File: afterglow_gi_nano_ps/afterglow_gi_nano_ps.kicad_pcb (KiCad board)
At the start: 2 copper layers, 84 x 134.5 mm, 70 parts, among them J1 Conn_02x17_Odd_Even, J2 POWER_CONN, J3 GI_WPC_J120, J4 GI_WPC_J121, J5 GI_CONN_J119, J6 Conn_01x12_Male, Q1 FQP30N06L, Q2 FQP30N06L, Q3 FQP30N06L, Q4 FQP30N06L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

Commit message: Added 5V stabilizing capacitor
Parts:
- added C9: 100uF, Capacitors_THT:CP_Radial_D8.0mm_P3.50mm, F.Cu at (119.5, 41.0)
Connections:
- REF** pad 1: (no net) -> GND (x2)

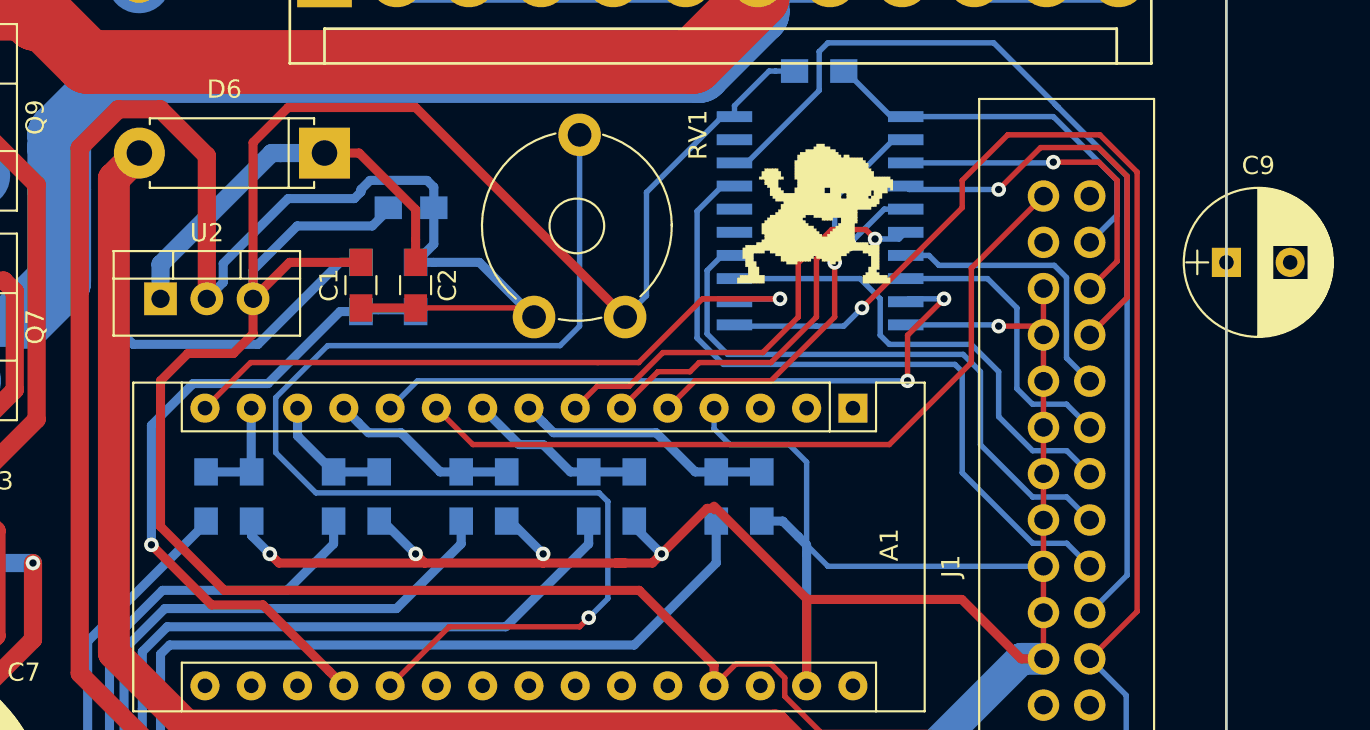
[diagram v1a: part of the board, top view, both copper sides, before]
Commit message: Added 5V stabilizing capacitor
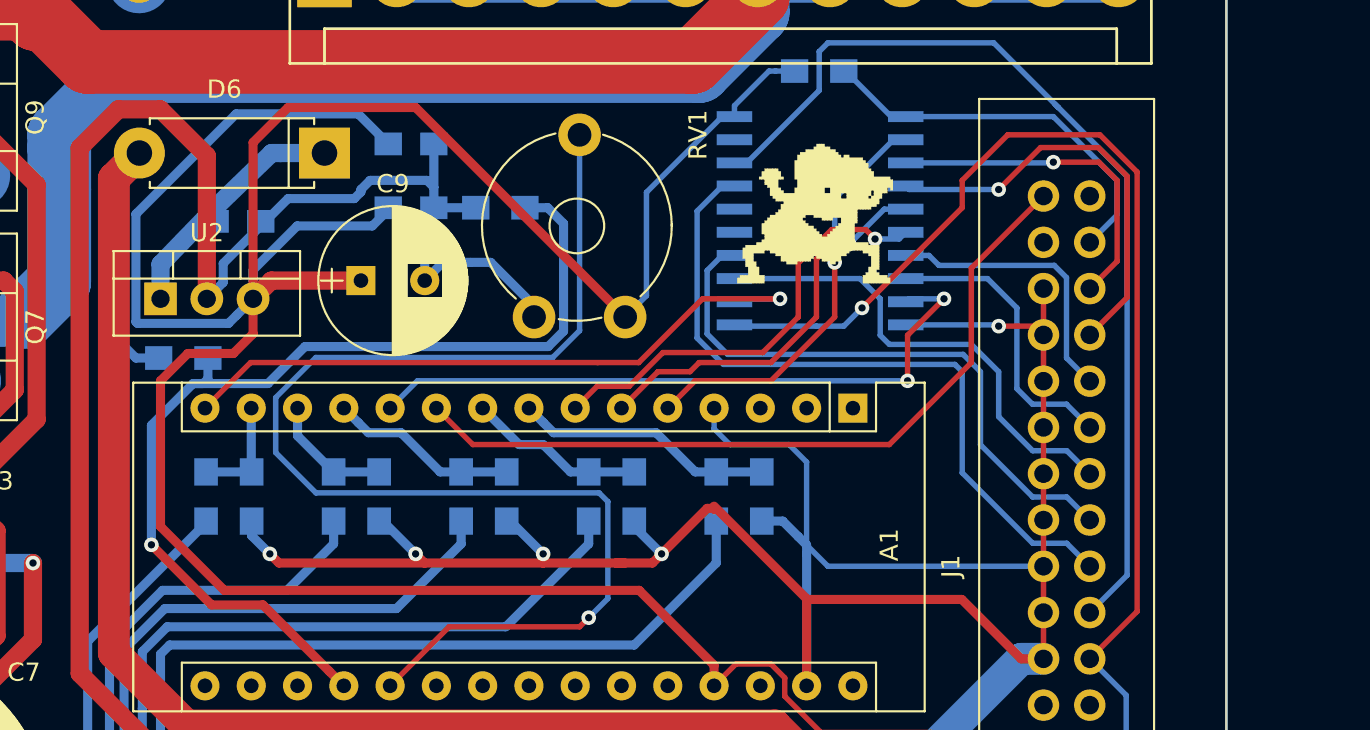
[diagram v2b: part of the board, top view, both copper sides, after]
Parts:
- C1, C2: moved to B.Cu
- moved C9 47.5 mm to (72.0, 42.0)
- moved R23 10.5 mm to (62.2, 46.2), turned to 0 degrees
- moved C2 10.4 mm to (65.2, 38.8), turned to 0 degrees
- moved C1 8.22 mm to (74.8, 34.5), turned to 180 degrees
- moved R24 6.37 mm to (79.7, 38.0), turned to 180 degrees
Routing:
- net /5V: track 152.7 -> 182.1 mm
- net Net-(A1-Pad19): track 37.4 -> 55.5 mm
- net +12V: track 574.0 -> 561.7 mm
- net Net-(C2-Pad1): track 22.6 -> 14.9 mm
- net GND: track 539.5 -> 535.8 mm

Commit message: Added PS BOM and schematic
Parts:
- C4: value C -> 1uF
- C5, C6, C7, C8: value CP -> 5600uF
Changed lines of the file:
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@@
       (effects (font (size 1 1) (thickness 0.15)))
     )
-    (fp_text value C (at 2.5 3.06 90) (layer F.Fab)
+    (fp_text value 1uF (at 2.5 3.06 90) (layer F.Fab)
       (effects (font (size 1 1) (thickness 0.15)))
     )
@@
       (effects (font (size 1 1) (thickness 0.15)))
     )
-    (fp_text value CP (at 3.75 10.31) (layer F.Fab)
+    (fp_text value 5600uF (at 3.75 10.31) (layer F.Fab)
       (effects (font (size 1 1) (thickness 0.15)))
     )
@@
       (effects (font (size 1 1) (thickness 0.15)))
     )
-    (fp_text value CP (at 3.75 10.31) (layer F.Fab)
+    (fp_text value 5600uF (at 3.75 10.31) (layer F.Fab)
       (effects (font (size 1 1) (thickness 0.15)))
     )
@@
       (effects (font (size 1 1) (thickness 0.15)))
     )
-    (fp_text value CP (at 3.75 10.31) (layer F.Fab)
+    (fp_text value 5600uF (at 3.75 10.31) (layer F.Fab)
       (effects (font (size 1 1) (thickness 0.15)))
     )
@@
       (effects (font (size 1 1) (thickness 0.15)))
     )
-    (fp_text value CP (at 3.75 10.31) (layer F.Fab)
-      (effects (font (size 1 1) (thickness 0.15)))
-    )
+    (fp_text value 5600uF (at 3.75 10.31) (layer F.Fab)
+      (effects (font (size 1 1) (thickness 0.15)))
+    )
